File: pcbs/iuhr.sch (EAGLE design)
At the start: 78 parts, among them Q1 20.000MHz

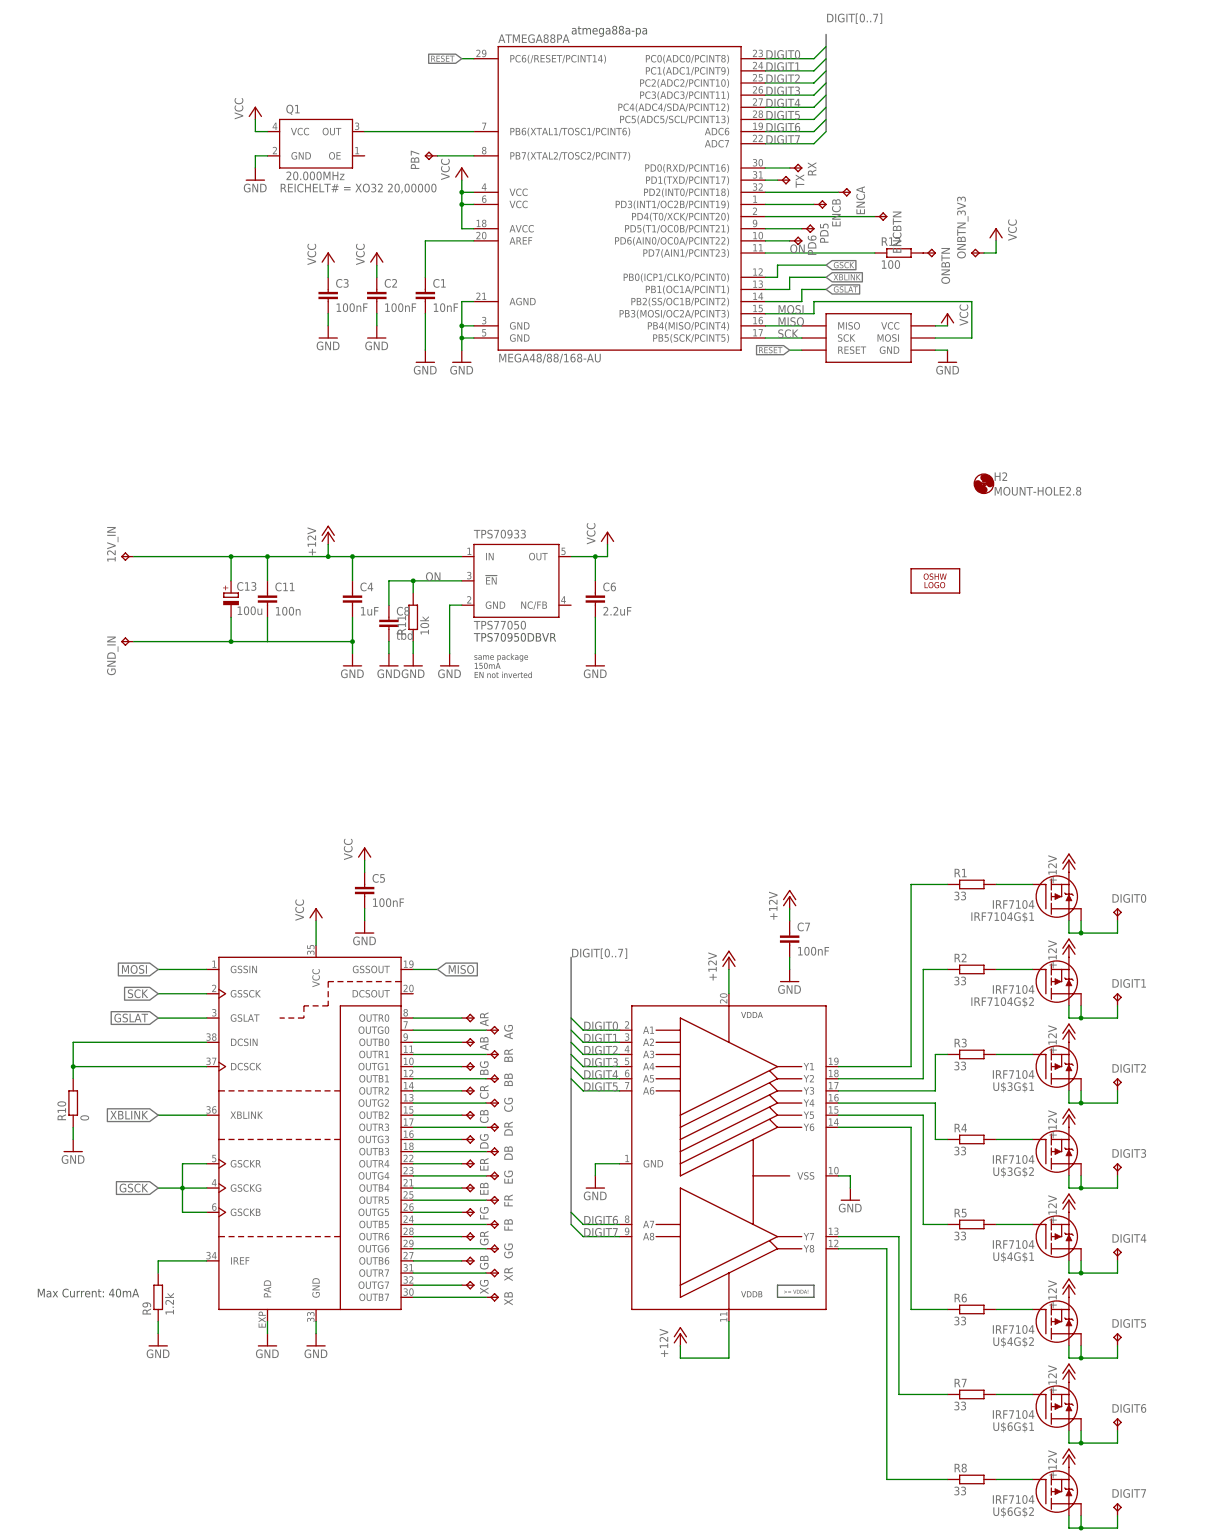
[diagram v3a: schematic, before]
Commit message: Add p-channel mosfet to be able to shut off 12V part.
TODO: find space on board
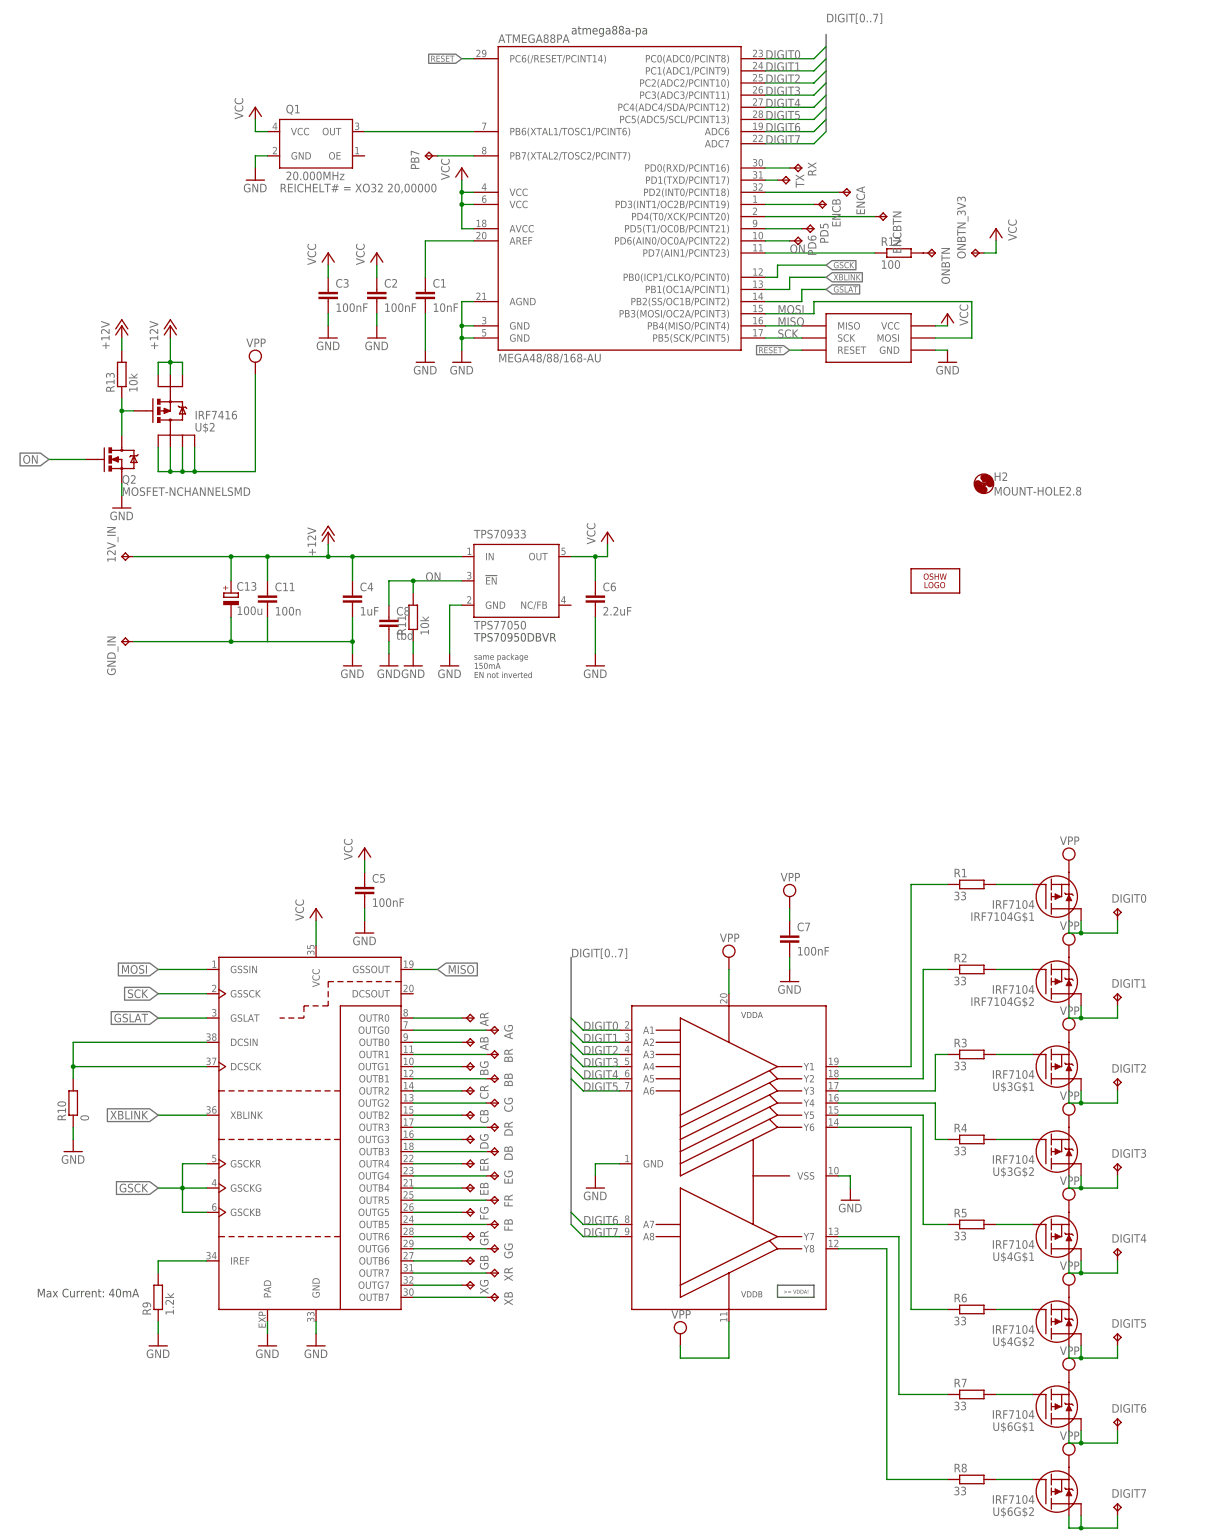
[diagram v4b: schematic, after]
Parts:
- added Q2: MOSFET-NCHANNELSMD, SparkFun:MOSFET-NCHANNELSMD
- added R13: 10k, resistor:R-EU_R0603
- added U$2: IRF7416, ShortCircuitRobotics:IRF7416
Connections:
- new net N$61: Q2.D, R13.1, U$2.G
- new net VPP: ADG3123.VDDA, ADG3123.VDDB, C7.1, IRF7104G$1.S, IRF7104G$2.S, U$2.D, U$2.D1, U$2.D2, U$2.D3, U$3G$1.S, U$3G$2.S, U$4G$1.S, U$4G$2.S, U$6G$1.S, U$6G$2.S
- net +12V: now also R13.2, U$2.S, U$2.S1, U$2.S2; no longer ADG3123.VDDA, ADG3123.VDDB, C7.1, IRF7104G$1.S, IRF7104G$2.S, U$3G$1.S, U$3G$2.S, U$4G$1.S, U$4G$2.S, U$6G$1.S, U$6G$2.S
- net GND: now also Q2.S
- net ON: now also Q2.G

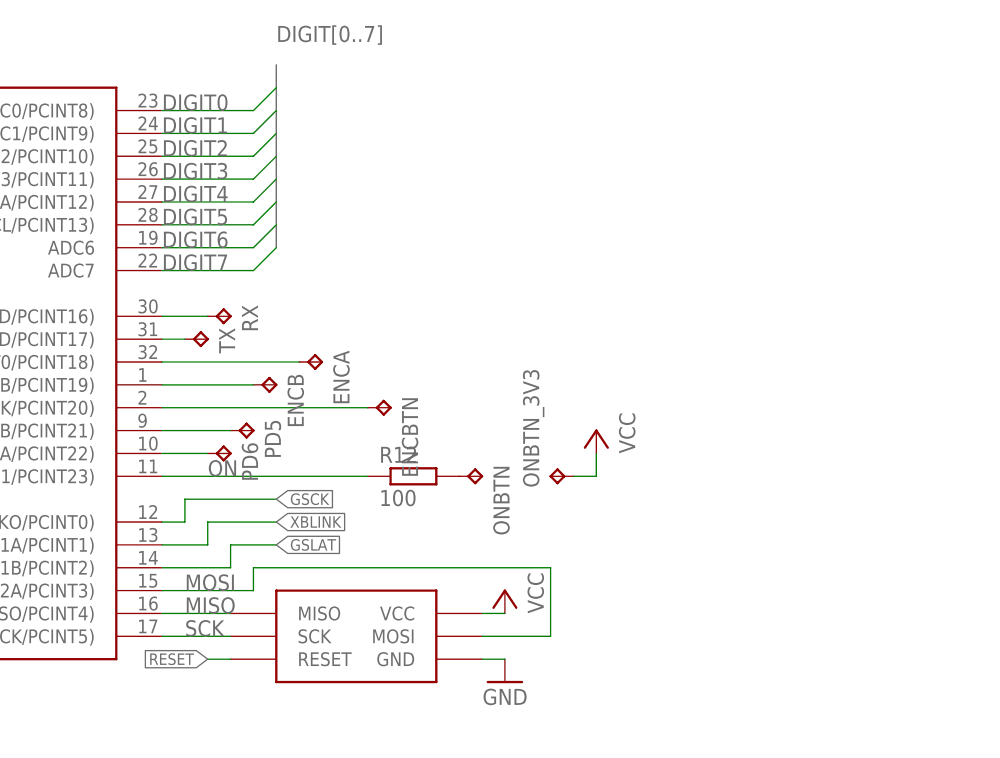
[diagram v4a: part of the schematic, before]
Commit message: correct power-on button and add detection
ToDo: - reassign DIGIT6
      - layout for this commit
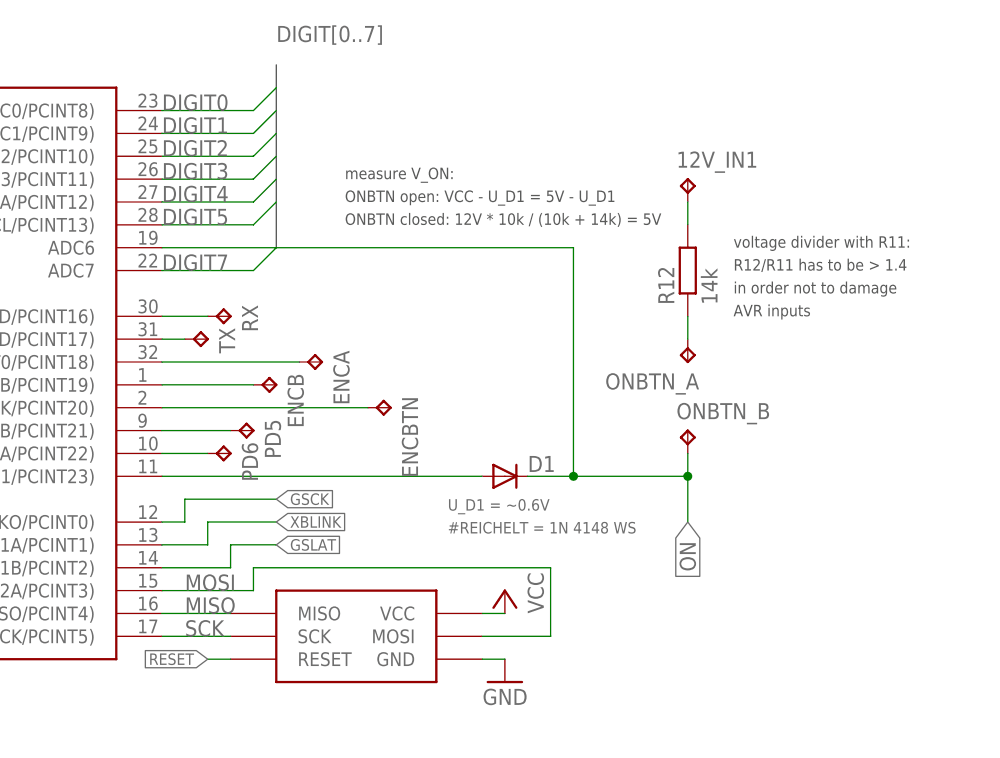
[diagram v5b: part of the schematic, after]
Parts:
- removed ONBTN, ONBTN_3V3: TPTP15SQ, testpad:TPTP15SQ
- added 12V_IN1: TPTP20SQ, testpad:TPTP20SQ
- added D1: (no value), diode:DIODE-SOD323-R
- added ONBTN_A, ONBTN_B: TPTP15SQ, testpad:TPTP15SQ
- R12: value 100 -> 14k
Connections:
- new net N$63: 12V_IN1.TP, R12.2
- new net N$64: ATMEGA88PA.PD7(AIN1/PCINT23), D1.A
- net DIGIT6: no longer ATMEGA88PA.ADC6
- net N$59: now also ONBTN_A.TP, R12.1; no longer ONBTN.TP, R12.2
- net ON: now also ATMEGA88PA.ADC6, D1.C, ONBTN_B.TP; no longer ATMEGA88PA.PD7(AIN1/PCINT23), R12.1
- net VCC: no longer ONBTN_3V3.TP
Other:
- note added: "AVR inputs"
- note added: "ONBTN closed: 12V * 10k / (10k + 14k) = 5V"
- note added: "ONBTN open: VCC - U_D1 = 5V - U_D1"
- note added: "R12/R11 has to be > 1.4"
- note added: "in order not to damage"
- note added: "measure V_ON:"
- note added: "voltage divider with R11:"
- moved on the sheet: R12
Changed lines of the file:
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@@
 <?xml version="1.0" encoding="utf-8"?>
 <!DOCTYPE eagle SYSTEM "eagle.dtd">
-<eagle version="6.5.0">
+<eagle version="6.4">
 <drawing>
 <settings>
@@
 <setting verticaltext="up"/>
 </settings>
-<grid distance="0.1" unitdist="inch" unit="inch" style="lines" multiple="1" display="no" altdistance="0.01" altunitdist="inch" altunit="inch"/>
+<grid distance="0.1" unitdist="inch" unit="inch" style="lines" multiple="1" display="no" altdistance="0.05" altunitdist="inch" altunit="inch"/>
 <layers>
 <layer number="1" name="Top" color="4" fill="1" visible="no" active="no"/>
@@
 <part name="GND32" library="supply1" deviceset="GND" device=""/>
 <part name="P+18" library="supply1" deviceset="VCC" device=""/>
-<part name="ONBTN" library="testpad" deviceset="TP" device="TP15SQ"/>
-<part name="ONBTN_3V3" library="testpad" deviceset="TP" device="TP15SQ"/>
-<part name="P+19" library="supply1" deviceset="VCC" device=""/>
+<part name="ONBTN_B" library="testpad" deviceset="TP" device="TP15SQ"/>
+<part name="ONBTN_A" library="testpad" deviceset="TP" device="TP15SQ"/>
 <part name="12V_IN" library="testpad" deviceset="TP" device="TP20SQ"/>
 <part name="GND_IN" library="testpad" deviceset="TP" device="TP20SQ"/>
@@
 <part name="C8" library="resistor" deviceset="C-EU" device="C0603" value="tbd"/>
 <part name="GND18" library="supply1" deviceset="GND" device=""/>
-<part name="R12" library="resistor" deviceset="R-EU_" device="R0603" value="100"/>
 <part name="U$2" library="ShortCircuitRobotics" deviceset="IRF7416" device=""/>
 <part name="P+22" library="supply1" deviceset="+12V" device=""/>
@@
 <part name="GND19" library="supply1" deviceset="GND" device=""/>
 <part name="Q2" library="SparkFun" deviceset="MOSFET-NCHANNEL" device="SMD"/>
+<part name="D1" library="diode" deviceset="DIODE-" device="SOD323-R">
+<attribute name="#REICHELT" value="1N 4148 WS"/>
+<attribute name="IDENTIFIER" value="1N4148-WS"/>
+<attribute name="U_D1" value="~0.6V"/>
+</part>
+<part name="R12" library="resistor" deviceset="R-EU_" device="R0603" value="14k"/>
+<part name="12V_IN1" library="testpad" deviceset="TP" device="TP20SQ"/>
 </parts>
 <sheets>
@@
 150mA
 EN not inverted</text>
+<text x="193.04" y="144.78" size="1.27" layer="97">measure V_ON:</text>
+<text x="193.04" y="142.24" size="1.27" layer="97">ONBTN open: VCC - U_D1 = 5V - U_D1</text>
+<text x="193.04" y="139.7" size="1.27" layer="97">ONBTN closed: 12V * 10k / (10k + 14k) = 5V</text>
+<text x="236.22" y="137.16" size="1.27" layer="97">voltage divider with R11:</text>
+<text x="236.22" y="134.62" size="1.27" layer="97">R12/R11 has to be &gt; 1.4</text>
+<text x="236.22" y="132.08" size="1.27" layer="97">in order not to damage</text>
+<text x="236.22" y="129.54" size="1.27" layer="97">AVR inputs</text>
 </plain>
 <instances>
@@
 <instance part="GND32" gate="1" x="66.04" y="127"/>
 <instance part="P+18" gate="VCC" x="66.04" y="142.24"/>
-<instance part="ONBTN" gate="G$1" x="208.28" y="111.76" rot="R270"/>
-<instance part="ONBTN_3V3" gate="G$1" x="215.9" y="111.76" rot="R90"/>
-<instance part="P+19" gate="VCC" x="220.98" y="116.84" rot="MR0"/>
+<instance part="ONBTN_B" gate="G$1" x="231.14" y="116.84"/>
+<instance part="ONBTN_A" gate="G$1" x="231.14" y="124.46" rot="R180"/>
 <instance part="12V_IN" gate="G$1" x="38.1" y="48.26" rot="R90"/>
 <instance part="GND_IN" gate="G$1" x="38.1" y="30.48" rot="MR270"/>
@@
 <instance part="C8" gate="G$1" x="93.98" y="35.56"/>
 <instance part="GND18" gate="1" x="93.98" y="25.4"/>
-<instance part="R12" gate="G$1" x="200.66" y="111.76"/>
 <instance part="U$2" gate="G$1" x="48.26" y="78.74" rot="MR180"/>
 <instance part="P+22" gate="1" x="48.26" y="96.52"/>
@@
 <attribute name="VALUE" x="38.1" y="60.96" size="1.778" layer="96"/>
 </instance>
+<instance part="D1" gate="G$1" x="210.82" y="111.76">
+<attribute name="IDENTIFIER" x="210.82" y="111.76" size="1.778" layer="96" display="off"/>
+<attribute name="#REICHELT" x="204.47" y="105.41" size="1.27" layer="96" display="both"/>
+<attribute name="U_D1" x="204.47" y="107.95" size="1.27" layer="96" display="both"/>
+</instance>
+<instance part="R12" gate="G$1" x="231.14" y="134.62" rot="R90"/>
+<instance part="12V_IN1" gate="G$1" x="231.14" y="144.78"/>
 </instances>
 <busses>
@@
 <pinref part="Q1" gate="G$1" pin="VCC"/>
 <pinref part="P+18" gate="VCC" pin="VCC"/>
-</segment>
-<segment>
-<pinref part="ONBTN_3V3" gate="G$1" pin="TP"/>
-<wire x1="218.44" y1="111.76" x2="220.98" y2="111.76" width="0.1524" layer="91"/>
-<wire x1="220.98" y1="111.76" x2="220.98" y2="114.3" width="0.1524" layer="91"/>
-<pinref part="P+19" gate="VCC" pin="VCC"/>
 </segment>
 <segment>
@@
 <label x="134.62" y="-91.44" size="1.778" layer="95"/>
 </segment>
-<segment>
-<pinref part="ATMEGA88PA" gate="1" pin="ADC6"/>
-<wire x1="185.42" y1="139.7" x2="182.88" y2="137.16" width="0.1524" layer="91"/>
-<wire x1="182.88" y1="137.16" x2="172.72" y2="137.16" width="0.1524" layer="91"/>
-<label x="172.72" y="137.16" size="1.778" layer="95"/>
-</segment>
 </net>
 <net name="DIGIT5" class="0">
@@
 </segment>
 <segment>
-<pinref part="ATMEGA88PA" gate="1" pin="PD7(AIN1/PCINT23)"/>
-<wire x1="172.72" y1="111.76" x2="195.58" y2="111.76" width="0.1524" layer="91"/>
-<label x="177.8" y="111.76" size="1.778" layer="95"/>
-<pinref part="R12" gate="G$1" pin="1"/>
-</segment>
-<segment>
 <pinref part="Q2" gate="G$1" pin="G"/>
 <wire x1="30.48" y1="68.58" x2="22.86" y2="68.58" width="0.1524" layer="91"/>
 <label x="22.86" y="68.58" size="1.778" layer="95" rot="MR0" xref="yes"/>
 </segment>
+<segment>
+<pinref part="ONBTN_B" gate="G$1" pin="TP"/>
+<wire x1="231.14" y1="114.3" x2="231.14" y2="111.76" width="0.1524" layer="91"/>
+<label x="231.14" y="106.68" size="1.778" layer="95" rot="R270" xref="yes"/>
+<pinref part="D1" gate="G$1" pin="C"/>
+<wire x1="231.14" y1="111.76" x2="231.14" y2="106.68" width="0.1524" layer="91"/>
+<wire x1="213.36" y1="111.76" x2="218.44" y2="111.76" width="0.1524" layer="91"/>
+<junction x="231.14" y="111.76"/>
+<pinref part="ATMEGA88PA" gate="1" pin="ADC6"/>
+<wire x1="218.44" y1="111.76" x2="231.14" y2="111.76" width="0.1524" layer="91"/>
+<wire x1="172.72" y1="137.16" x2="218.44" y2="137.16" width="0.1524" layer="91"/>
+<wire x1="218.44" y1="137.16" x2="218.44" y2="111.76" width="0.1524" layer="91"/>
+<junction x="218.44" y="111.76"/>
+</segment>
 </net>
 <net name="N$7" class="0">
@@
 <pinref part="PB7" gate="G$1" pin="TP"/>
 <wire x1="104.14" y1="132.08" x2="111.76" y2="132.08" width="0.1524" layer="91"/>
-</segment>
-</net>
-<net name="N$59" class="0">
-<segment>
-<pinref part="ONBTN" gate="G$1" pin="TP"/>
-<pinref part="R12" gate="G$1" pin="2"/>
 </segment>
 </net>
@@
 </segment>
 </net>
+<net name="N$59" class="0">
+<segment>
+<pinref part="ONBTN_A" gate="G$1" pin="TP"/>
+<pinref part="R12" gate="G$1" pin="1"/>
+<wire x1="231.14" y1="129.54" x2="231.14" y2="127" width="0.1524" layer="91"/>
+</segment>
+</net>
+<net name="N$63" class="0">
+<segment>
+<pinref part="R12" gate="G$1" pin="2"/>
+<pinref part="12V_IN1" gate="G$1" pin="TP"/>
+<wire x1="231.14" y1="142.24" x2="231.14" y2="139.7" width="0.1524" layer="91"/>
+</segment>
+</net>
+<net name="N$64" class="0">
+<segment>
+<pinref part="ATMEGA88PA" gate="1" pin="PD7(AIN1/PCINT23)"/>
+<pinref part="D1" gate="G$1" pin="A"/>
+<wire x1="172.72" y1="111.76" x2="208.28" y2="111.76" width="0.1524" layer="91"/>
+</segment>
+</net>
